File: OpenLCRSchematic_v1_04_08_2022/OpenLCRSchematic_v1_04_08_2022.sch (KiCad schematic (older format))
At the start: 18 parts

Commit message: Measurement Circuit Update
Update measurement circuit
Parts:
- removed U?: TLC7528CN, DIP254P762X508-20, symbol TLC7528CN:TLC7528CN
- removed U?: MCP6294-E_SL, SOIC127P600X175-14N, symbol MCP6294-E_SL:MCP6294-E_SL
- removed U?: CD74HCT4066M, SOIC127P600X175-14N, symbol CD74HCT4066M:CD74HCT4066M
- removed U?: MCP6S91-E_P, DIP787W46P254L927H533Q8, symbol MCP6S91-E_P:MCP6S91-E_P
- removed U?: INA217AIP, DIP794W45P254L959H508Q8, symbol INA217AIP:INA217AIP
- gave numbers to parts that had none: 13
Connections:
- net labels added: +3.3V, +BATT, 3.3V
- wire segments 66 -> 67
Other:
- note added: "Measurement Circuit"
- note added: "Note: 3.3V is generated by a\nlinear regulator on the Teensy \n4.1 board derived from 5V."
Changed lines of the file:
@@
 $Descr A4 11693 8268
 encoding utf-8
-Sheet 1 1
+Sheet 1 2
 Title "OpenLCR Measurement Circuitry"
 Date ""
@@
 $EndDescr
 $Comp
-L TLC7528CN:TLC7528CN U?
-U 1 1 6250931A
-P 17700 4750
-F 0 "U?" H 17700 6020 50  0000 C CNN
-F 1 "TLC7528CN" H 17700 5929 50  0000 C CNN
-F 2 "DIP254P762X508-20" H 17700 4750 50  0001 L BNN
-F 3 "" H 17700 4750 50  0001 L BNN
-F 4 "PDIP-20" H 17700 4750 50  0001 L BNN "PACKAGE"
-F 5 "36K3648" H 17700 4750 50  0001 L BNN "OC_NEWARK"
-F 6 "TLC7528CN" H 17700 4750 50  0001 L BNN "MPN"
-F 7 "8454647" H 17700 4750 50  0001 L BNN "OC_FARNELL"
-F 8 "Texas Instruments" H 17700 4750 50  0001 L BNN "SUPPLIER"
-	1    17700 4750
-	1    0    0    -1
-$EndComp
-$Comp
-L MCP6294-E_SL:MCP6294-E_SL U?
-U 1 1 6250B959
-P 19950 4500
-F 0 "U?" H 19950 5370 50  0000 C CNN
-F 1 "MCP6294-E_SL" H 19950 5279 50  0000 C CNN
-F 2 "SOIC127P600X175-14N" H 19950 4500 50  0001 L BNN
-F 3 "" H 19950 4500 50  0001 L BNN
-	1    19950 4500
-	1    0    0    -1
-$EndComp
-$Comp
-L CD74HCT4066M:CD74HCT4066M U?
-U 1 1 6250CB78
-P 19950 6250
-F 0 "U?" H 19950 7120 50  0000 C CNN
-F 1 "CD74HCT4066M" H 19950 7029 50  0000 C CNN
-F 2 "SOIC127P600X175-14N" H 19950 6250 50  0001 L BNN
-F 3 "" H 19950 6250 50  0001 L BNN
-	1    19950 6250
-	1    0    0    -1
-$EndComp
-$Comp
-L MCP6S91-E_P:MCP6S91-E_P U?
-U 1 1 6250E62B
-P 19950 2400
-F 0 "U?" H 19950 3170 50  0000 C CNN
-F 1 "MCP6S91-E_P" H 19950 3079 50  0000 C CNN
-F 2 "DIP787W46P254L927H533Q8" H 19950 2400 50  0001 L BNN
-F 3 "" H 19950 2400 50  0001 L BNN
-	1    19950 2400
-	1    0    0    -1
-$EndComp
-$Comp
-L INA217AIP:INA217AIP U?
-U 1 1 6250F06B
-P 23600 3850
-F 0 "U?" H 23600 4620 50  0000 C CNN
-F 1 "INA217AIP" H 23600 4529 50  0000 C CNN
-F 2 "DIP794W45P254L959H508Q8" H 23600 3850 50  0001 L BNN
-F 3 "" H 23600 3850 50  0001 L BNN
-	1    23600 3850
-	1    0    0    -1
-$EndComp
-$Comp
-L MAX680CPA_:MAX680CPA+ U?
+L MAX680CPA_:MAX680CPA+ U2
 U 1 1 6250FB8A
 P 2000 3850
-F 0 "U?" H 2000 4620 50  0000 C CNN
+F 0 "U2" H 2000 4620 50  0000 C CNN
 F 1 "MAX680CPA+" H 2000 4529 50  0000 C CNN
 F 2 "DIP794W47P254L991H457Q8" H 2000 3850 50  0001 L BNN
@@
 $EndComp
 $Comp
-L LiPoCharger_Booster:LiPoChargeBoost U?
+L LiPoCharger_Booster:LiPoChargeBoost U1
 U 1 1 62518618
 P 3000 2400
-F 0 "U?" H 3000 2725 50  0000 C CNN
+F 0 "U1" H 3000 2725 50  0000 C CNN
 F 1 "LiPoChargeBoost" H 3000 2634 50  0000 C CNN
 F 2 "" H 3000 2700 50  0001 C CNN
@@
 Lithium-Polymer Battery\n3.7V-4.2V, 2500mAh\nContains internal\nprotection circuitry
 $Comp
-L Device:Battery_Cell BT?
+L Device:Battery_Cell BT1
 U 1 1 62515AE1
 P 1650 2500
-F 0 "BT?" H 1768 2596 50  0000 L CNN
+F 0 "BT1" H 1768 2596 50  0000 L CNN
 F 1 "Battery_Cell" H 1768 2505 50  0000 L CNN
 F 2 "" V 1650 2560 50  0001 C CNN
@@
 	3600 2300 4150 2300
 $Comp
-L MAX680CPA_:MAX680CPA+ U?
+L MAX680CPA_:MAX680CPA+ U3
 U 1 1 6251CE4F
 P 2000 5300
-F 0 "U?" H 2000 6070 50  0000 C CNN
+F 0 "U3" H 2000 6070 50  0000 C CNN
 F 1 "MAX680CPA+" H 2000 5979 50  0000 C CNN
 F 2 "DIP794W47P254L991H457Q8" H 2000 5300 50  0001 L BNN
@@
 $EndComp
 $Comp
-L MAX680CPA_:MAX680CPA+ U?
+L MAX680CPA_:MAX680CPA+ U4
 U 1 1 6251D7F3
 P 2000 6800
-F 0 "U?" H 2000 7570 50  0000 C CNN
+F 0 "U4" H 2000 7570 50  0000 C CNN
 F 1 "MAX680CPA+" H 2000 7479 50  0000 C CNN
 F 2 "DIP794W47P254L991H457Q8" H 2000 6800 50  0001 L BNN
@@
 GND
 $Comp
-L power:+5V #PWR?
+L power:+5V #PWR03
 U 1 1 6251E328
 P 4300 2400
-F 0 "#PWR?" H 4300 2250 50  0001 C CNN
+F 0 "#PWR03" H 4300 2250 50  0001 C CNN
 F 1 "+5V" H 4315 2573 50  0000 C CNN
 F 2 "" H 4300 2400 50  0001 C CNN
@@
 $EndComp
 $Comp
-L power:GND #PWR?
+L power:GND #PWR04
 U 1 1 6251ED8F
 P 4300 2500
-F 0 "#PWR?" H 4300 2250 50  0001 C CNN
+F 0 "#PWR04" H 4300 2250 50  0001 C CNN
 F 1 "GND" H 4305 2327 50  0000 C CNN
 F 2 "" H 4300 2500 50  0001 C CNN
@@
 	3600 2500 4300 2500
 $Comp
-L power:GND #PWR?
+L power:GND #PWR09
 U 1 1 6251F89D
 P 2850 4250
-F 0 "#PWR?" H 2850 4000 50  0001 C CNN
+F 0 "#PWR09" H 2850 4000 50  0001 C CNN
 F 1 "GND" H 2855 4077 50  0000 C CNN
 F 2 "" H 2850 4250 50  0001 C CNN
@@
 $EndComp
 $Comp
-L power:GND #PWR?
+L power:GND #PWR011
 U 1 1 625204F9
 P 2850 5700
-F 0 "#PWR?" H 2850 5450 50  0001 C CNN
+F 0 "#PWR011" H 2850 5450 50  0001 C CNN
 F 1 "GND" H 2855 5527 50  0000 C CNN
 F 2 "" H 2850 5700 50  0001 C CNN
@@
 $EndComp
 $Comp
-L power:GND #PWR?
+L power:GND #PWR013
 U 1 1 625209A4
 P 2850 7200
-F 0 "#PWR?" H 2850 6950 50  0001 C CNN
+F 0 "#PWR013" H 2850 6950 50  0001 C CNN
 F 1 "GND" H 2855 7027 50  0000 C CNN
 F 2 "" H 2850 7200 50  0001 C CNN
@@
 $EndComp
 $Comp
-L power:+5V #PWR?
+L power:+5V #PWR012
 U 1 1 62520C44
 P 2850 6400
-F 0 "#PWR?" H 2850 6250 50  0001 C CNN
+F 0 "#PWR012" H 2850 6250 50  0001 C CNN
 F 1 "+5V" H 2865 6573 50  0000 C CNN
 F 2 "" H 2850 6400 50  0001 C CNN
@@
 $EndComp
 $Comp
-L power:+5V #PWR?
+L power:+5V #PWR010
 U 1 1 62521D7D
 P 2850 4900
-F 0 "#PWR?" H 2850 4750 50  0001 C CNN
+F 0 "#PWR010" H 2850 4750 50  0001 C CNN
 F 1 "+5V" H 2865 5073 50  0000 C CNN
 F 2 "" H 2850 4900 50  0001 C CNN
@@
 $EndComp
 $Comp
-L power:+5V #PWR?
+L power:+5V #PWR06
 U 1 1 62521EFB
 P 2850 3450
-F 0 "#PWR?" H 2850 3300 50  0001 C CNN
+F 0 "#PWR06" H 2850 3300 50  0001 C CNN
 F 1 "+5V" H 2865 3623 50  0000 C CNN
 F 2 "" H 2850 3450 50  0001 C CNN
@@
 -10V
 $Comp
-L power:GND #PWR?
+L power:GND #PWR07
 U 1 1 62527CB2
 P 3200 3650
-F 0 "#PWR?" H 3200 3400 50  0001 C CNN
+F 0 "#PWR07" H 3200 3400 50  0001 C CNN
 F 1 "GND" H 3205 3477 50  0000 C CNN
 F 2 "" H 3200 3650 50  0001 C CNN
@@
 	3200 3650 3500 3650
 $Comp
-L Device:CP C?
+L Device:CP C1
 U 1 1 6252898D
 P 3500 3400
-F 0 "C?" H 3618 3446 50  0000 L CNN
+F 0 "C1" H 3618 3446 50  0000 L CNN
 F 1 "10u" H 3618 3355 50  0000 L CNN
 F 2 "" H 3538 3250 50  0001 C CNN
@@
 $EndComp
 $Comp
-L Device:CP C?
+L Device:CP C3
 U 1 1 6252958A
 P 3500 3900
-F 0 "C?" H 3618 3946 50  0000 L CNN
+F 0 "C3" H 3618 3946 50  0000 L CNN
 F 1 "10u" H 3618 3855 50  0000 L CNN
 F 2 "" H 3538 3750 50  0001 C CNN
@@
 	3500 3250 3500 3150
 $Comp
-L Device:CP C?
+L Device:CP C2
 U 1 1 6252C5D6
 P 1150 3700
-F 0 "C?" H 950 3750 50  0000 L CNN
+F 0 "C2" H 950 3750 50  0000 L CNN
 F 1 "10u" H 900 3650 50  0000 L CNN
 F 2 "" H 1188 3550 50  0001 C CNN
@@
 $EndComp
 $Comp
-L Device:CP C?
+L Device:CP C4
 U 1 1 625314A6
 P 950 4000
-F 0 "C?" H 750 4050 50  0000 L CNN
+F 0 "C4" H 750 4050 50  0000 L CNN
 F 1 "10u" H 700 3950 50  0000 L CNN
 F 2 "" H 988 3850 50  0001 C CNN
@@
 	1100 4050 1300 4050
 $Comp
-L Device:CP C?
+L Device:CP C5
 U 1 1 62535813
 P 1150 5150
-F 0 "C?" H 950 5200 50  0000 L CNN
+F 0 "C5" H 950 5200 50  0000 L CNN
 F 1 "10u" H 900 5100 50  0000 L CNN
 F 2 "" H 1188 5000 50  0001 C CNN
@@
 $EndComp
 $Comp
-L Device:CP C?
+L Device:CP C6
 U 1 1 62535819
 P 950 5450
-F 0 "C?" H 750 5500 50  0000 L CNN
+F 0 "C6" H 750 5500 50  0000 L CNN
 F 1 "10u" H 700 5400 50  0000 L CNN
 F 2 "" H 988 5300 50  0001 C CNN
@@
 	1100 5500 1300 5500
 $Comp
-L Device:CP C?
+L Device:CP C7
 U 1 1 62537749
 P 1150 6650
-F 0 "C?" H 950 6700 50  0000 L CNN
+F 0 "C7" H 950 6700 50  0000 L CNN
 F 1 "10u" H 900 6600 50  0000 L CNN
 F 2 "" H 1188 6500 50  0001 C CNN
@@
 $EndComp
 $Comp
-L Device:CP C?
+L Device:CP C8
 U 1 1 6253774F
 P 950 6950
-F 0 "C?" H 750 7000 50  0000 L CNN
+F 0 "C8" H 750 7000 50  0000 L CNN
 F 1 "10u" H 700 6900 50  0000 L CNN
 F 2 "" H 988 6800 50  0001 C CNN
@@
 	4550 7750 4550 500
 Wire Notes Line width 39
-	4550 500  500  500
+	500  7750 4550 7750
+Wire Wire Line
+	3500 1600 4000 1600
+Text Label 3650 1600 0    50   ~ 0
+3.3V
+Text Notes 3200 1900 0    50   ~ 0
+Note:  3.3V is generated by a\nlinear regulator on the Teensy \n4.1 board derived from 5V.
+$Comp
+L power:+3.3V #PWR01
+U 1 1 6259A3DF
+P 4000 1600
+F 0 "#PWR01" H 4000 1450 50  0001 C CNN
+F 1 "+3.3V" H 4015 1773 50  0000 C CNN
+F 2 "" H 4000 1600 50  0001 C CNN
+F 3 "" H 4000 1600 50  0001 C CNN
+	1    4000 1600
+	1    0    0    -1
+$EndComp
+$Sheet
+S 4700 1050 6350 1700
+U 625D4E84
+F0 "Measurement Circuit" 50
+F1 "MeasurementCircuit.sch" 50
+$EndSheet
+Text Notes 4700 850  0    157  ~ 31
+Measurement Circuit
 Wire Notes Line width 39
-	500  7750 4550 7750
+	11150 2900 4550 2900
+Wire Notes Line width 39
+	11150 500  11150 2900
+Wire Notes Line width 39
+	500  500  11150 500
+$Comp
+L power:+10V #PWR05
+U 1 1 625FFB3F
+P 3500 3150
+F 0 "#PWR05" H 3500 3000 50  0001 C CNN
+F 1 "+10V" H 3515 3323 50  0000 C CNN
+F 2 "" H 3500 3150 50  0001 C CNN
+F 3 "" H 3500 3150 50  0001 C CNN
+	1    3500 3150
+	1    0    0    -1
+$EndComp
+Connection ~ 3500 3150
+$Comp
+L power:-10V #PWR08
+U 1 1 6260017C
+P 3500 4150
+F 0 "#PWR08" H 3500 4250 50  0001 C CNN
+F 1 "-10V" H 3515 4323 50  0000 C CNN
+F 2 "" H 3500 4150 50  0001 C CNN
+F 3 "" H 3500 4150 50  0001 C CNN
+	1    3500 4150
+	-1   0    0    1
+$EndComp
+Connection ~ 3500 4150
+$Comp
+L power:+BATT #PWR02
+U 1 1 626C0E5D
+P 4150 2300
+F 0 "#PWR02" H 4150 2150 50  0001 C CNN
+F 1 "+BATT" H 4165 2473 50  0000 C CNN
+F 2 "" H 4150 2300 50  0001 C CNN
+F 3 "" H 4150 2300 50  0001 C CNN
+	1    4150 2300
+	1    0    0    -1
+$EndComp
 $EndSCHEMATC

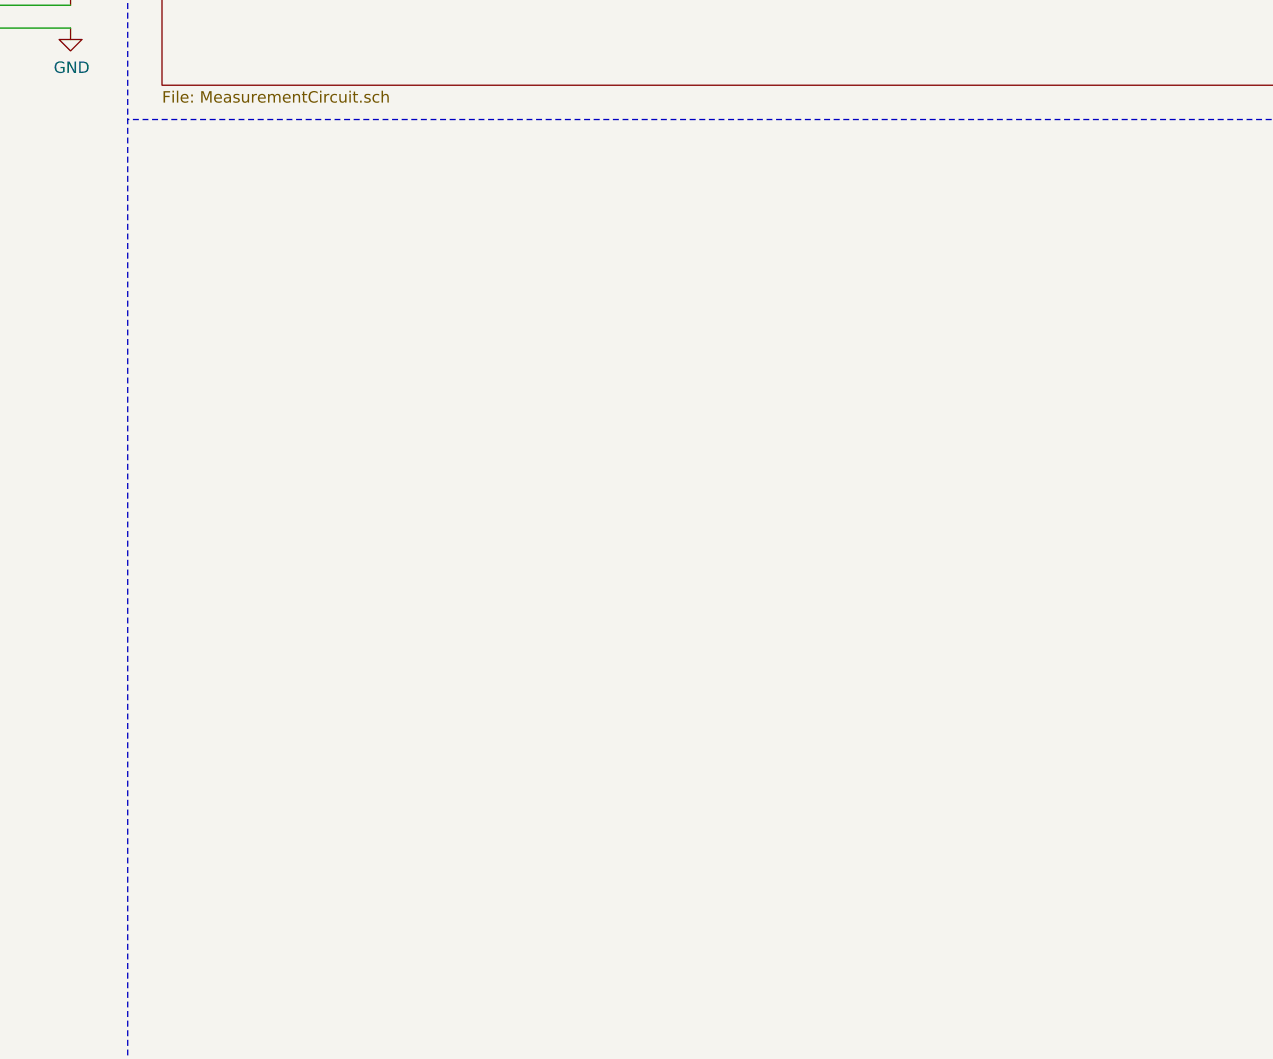
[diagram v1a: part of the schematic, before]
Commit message: Make Teensy 4.1 symbol
Add the Teensy 4.1 circuit symbol to the schematic.  Still not exactly sure on what pin assignments I'll use.
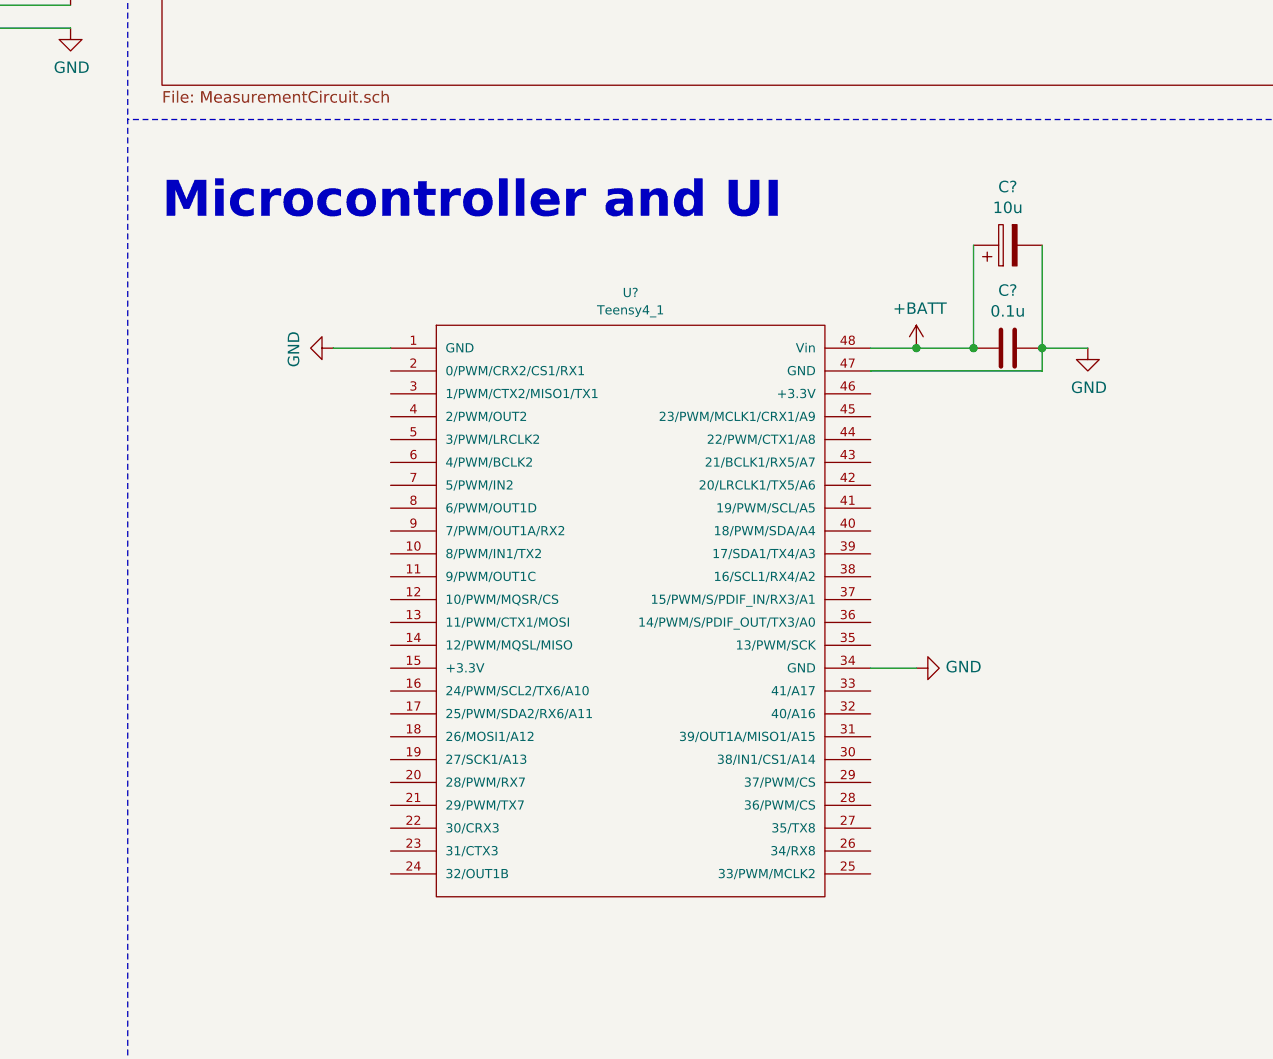
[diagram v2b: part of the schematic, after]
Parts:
- added C?: 10u, symbol Device:CP
- added C?: 0.1u, symbol Device:C
- added U?: Teensy4_1, symbol Teensy4_1:Teensy4_1
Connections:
- wire segments 67 -> 76
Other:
- note added: "Microcontroller and UI"
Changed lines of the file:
@@
 	1    0    0    -1
 $EndComp
+$Comp
+L Teensy4_1:Teensy4_1 U?
+U 1 1 6299E2B7
+P 6750 5150
+F 0 "U?" H 6750 6642 40  0000 C CNN
+F 1 "Teensy4_1" H 6750 6566 40  0000 C CNN
+F 2 "" H 6750 6550 40  0001 C CNN
+F 3 "" H 6750 6550 40  0001 C CNN
+	1    6750 5150
+	1    0    0    -1
+$EndComp
+Text Notes 4700 3350 0    157  ~ 31
+Microcontroller and UI
+$Comp
+L power:+BATT #PWR?
+U 1 1 629A203F
+P 8000 3900
+F 0 "#PWR?" H 8000 3750 50  0001 C CNN
+F 1 "+BATT" H 8015 4073 50  0000 C CNN
+F 2 "" H 8000 3900 50  0001 C CNN
+F 3 "" H 8000 3900 50  0001 C CNN
+	1    8000 3900
+	1    0    0    -1
+$EndComp
+$Comp
+L Device:CP C?
+U 1 1 629A283D
+P 8400 3450
+F 0 "C?" V 8655 3450 50  0000 C CNN
+F 1 "10u" V 8564 3450 50  0000 C CNN
+F 2 "" H 8438 3300 50  0001 C CNN
+F 3 "~" H 8400 3450 50  0001 C CNN
+	1    8400 3450
+	0    -1   -1   0
+$EndComp
+$Comp
+L Device:C C?
+U 1 1 629A3784
+P 8400 3900
+F 0 "C?" V 8148 3900 50  0000 C CNN
+F 1 "0.1u" V 8239 3900 50  0000 C CNN
+F 2 "" H 8438 3750 50  0001 C CNN
+F 3 "~" H 8400 3900 50  0001 C CNN
+	1    8400 3900
+	0    1    1    0
+$EndComp
+$Comp
+L power:GND #PWR?
+U 1 1 629A5333
+P 8750 3900
+F 0 "#PWR?" H 8750 3650 50  0001 C CNN
+F 1 "GND" H 8755 3727 50  0000 C CNN
+F 2 "" H 8750 3900 50  0001 C CNN
+F 3 "" H 8750 3900 50  0001 C CNN
+	1    8750 3900
+	1    0    0    -1
+$EndComp
+Wire Wire Line
+	8250 3900 8000 3900
+Wire Wire Line
+	8000 3900 7800 3900
+Connection ~ 8000 3900
+Wire Wire Line
+	8250 3900 8250 3450
+Connection ~ 8250 3900
+Wire Wire Line
+	8550 3450 8550 3900
+Wire Wire Line
+	8550 3900 8750 3900
+Connection ~ 8550 3900
+$Comp
+L power:GND #PWR?
+U 1 1 629ADD22
+P 5450 3900
+F 0 "#PWR?" H 5450 3650 50  0001 C CNN
+F 1 "GND" H 5455 3727 50  0000 C CNN
+F 2 "" H 5450 3900 50  0001 C CNN
+F 3 "" H 5450 3900 50  0001 C CNN
+	1    5450 3900
+	0    1    1    0
+$EndComp
+Wire Wire Line
+	7800 4000 8550 4000
+Wire Wire Line
+	8550 4000 8550 3900
+$Comp
+L power:GND #PWR?
+U 1 1 629B1BE9
+P 8000 5300
+F 0 "#PWR?" H 8000 5050 50  0001 C CNN
+F 1 "GND" V 8005 5172 50  0000 R CNN
+F 2 "" H 8000 5300 50  0001 C CNN
+F 3 "" H 8000 5300 50  0001 C CNN
+	1    8000 5300
+	0    -1   -1   0
+$EndComp
+Wire Wire Line
+	8000 5300 7800 5300
+Wire Wire Line
+	5450 3900 5700 3900
 $EndSCHEMATC

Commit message: Add Connections to Microcontroller
Add ILI9341 display and microcontroller connections.
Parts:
- added R?: 100, symbol Device:R_US
- added U?: ILI9341_Display, symbol ILI9341_Display_Module:ILI9341_Display
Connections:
- net labels added: CURRENT_MONITOR_SIGNAL_TO_ADC, D0, D1, D2, D3, D4, D5, D6, D7, DACSelAbar, DAC_CSbar, DAC_OUTPUT_MONITOR_SIGNAL_TO_ADC, DAC_WRbar, DISPLAY_CS, DISPLAY_DC, DISPLAY_MISO, DISPLAY_MOSI, DISPLAY_SCK, PGA_MOSI, PGA_SCK, PGA_~CS, SW1EN, SW2EN, SW3EN, SW4EN, SW5EN, SW6EN, SW7EN, SW8EN, TOUCHSCREEN_CS, TOUCHSCREEN_IRQ, VOLTAGE_MONITOR_SIGNAL_TO_ADC
- wire segments 76 -> 134

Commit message: Update Readme
Update readme with a short description of the design
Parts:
- gave numbers to parts that had none: 5
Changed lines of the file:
@@
 $EndComp
 $Comp
-L Teensy4_1:Teensy4_1 U?
+L Teensy4_1:Teensy4_1 U12
 U 1 1 6299E2B7
 P 6750 5150
-F 0 "U?" H 6750 6642 40  0000 C CNN
+F 0 "U12" H 6750 6642 40  0000 C CNN
 F 1 "Teensy4_1" H 6750 6566 40  0000 C CNN
 F 2 "" H 6750 6550 40  0001 C CNN
@@
 Microcontroller and UI
 $Comp
-L power:+BATT #PWR?
+L power:+BATT #PWR054
 U 1 1 629A203F
 P 8000 3900
-F 0 "#PWR?" H 8000 3750 50  0001 C CNN
+F 0 "#PWR054" H 8000 3750 50  0001 C CNN
 F 1 "+BATT" H 8015 4073 50  0000 C CNN
 F 2 "" H 8000 3900 50  0001 C CNN
@@
 $EndComp
 $Comp
-L Device:CP C?
+L Device:CP C21
 U 1 1 629A283D
 P 8400 3450
-F 0 "C?" V 8655 3450 50  0000 C CNN
+F 0 "C21" V 8655 3450 50  0000 C CNN
 F 1 "10u" V 8564 3450 50  0000 C CNN
 F 2 "" H 8438 3300 50  0001 C CNN
@@
 $EndComp
 $Comp
-L Device:C C?
+L Device:C C22
 U 1 1 629A3784
 P 8400 3900
-F 0 "C?" V 8148 3900 50  0000 C CNN
+F 0 "C22" V 8148 3900 50  0000 C CNN
 F 1 "0.1u" V 8239 3900 50  0000 C CNN
 F 2 "" H 8438 3750 50  0001 C CNN
@@
 $EndComp
 $Comp
-L power:GND #PWR?
+L power:GND #PWR055
 U 1 1 629A5333
 P 8750 3900
-F 0 "#PWR?" H 8750 3650 50  0001 C CNN
+F 0 "#PWR055" H 8750 3650 50  0001 C CNN
 F 1 "GND" H 8755 3727 50  0000 C CNN
 F 2 "" H 8750 3900 50  0001 C CNN
@@
 Connection ~ 8550 3900
 $Comp
-L power:GND #PWR?
+L power:GND #PWR053
 U 1 1 629ADD22
 P 5600 3900
-F 0 "#PWR?" H 5600 3650 50  0001 C CNN
+F 0 "#PWR053" H 5600 3650 50  0001 C CNN
 F 1 "GND" H 5605 3727 50  0000 C CNN
 F 2 "" H 5600 3900 50  0001 C CNN
@@
 	8550 4000 8550 3900
 $Comp
-L power:GND #PWR?
+L power:GND #PWR061
 U 1 1 629B1BE9
 P 8000 5300
-F 0 "#PWR?" H 8000 5050 50  0001 C CNN
+F 0 "#PWR061" H 8000 5050 50  0001 C CNN
 F 1 "GND" V 8005 5172 50  0000 R CNN
 F 2 "" H 8000 5300 50  0001 C CNN
@@
 	8000 5300 7800 5300
 $Comp
-L ILI9341_Display_Module:ILI9341_Display U?
+L ILI9341_Display_Module:ILI9341_Display U13
 U 1 1 629BBAF9
 P 10750 5550
-F 0 "U?" H 10700 6500 40  0000 L CNN
+F 0 "U13" H 10700 6500 40  0000 L CNN
 F 1 "ILI9341_Display" H 10500 6400 40  0000 L CNN
 F 2 "" H 10750 6350 40  0001 C CNN
@@
 $EndComp
 $Comp
-L power:+BATT #PWR?
+L power:+BATT #PWR057
 U 1 1 629BD32A
 P 10100 4900
-F 0 "#PWR?" H 10100 4750 50  0001 C CNN
+F 0 "#PWR057" H 10100 4750 50  0001 C CNN
 F 1 "+BATT" H 10115 5073 50  0000 C CNN
 F 2 "" H 10100 4900 50  0001 C CNN
@@
 $EndComp
 $Comp
-L power:GND #PWR?
+L power:GND #PWR058
 U 1 1 629BD7C1
 P 10100 5000
-F 0 "#PWR?" H 10100 4750 50  0001 C CNN
+F 0 "#PWR058" H 10100 4750 50  0001 C CNN
 F 1 "GND" V 10105 4872 50  0000 R CNN
 F 2 "" H 10100 5000 50  0001 C CNN
@@
 	10200 5100 9500 5100
 $Comp
-L power:+3.3V #PWR?
+L power:+3.3V #PWR056
 U 1 1 629D4F96
 P 8000 4100
-F 0 "#PWR?" H 8000 3950 50  0001 C CNN
+F 0 "#PWR056" H 8000 3950 50  0001 C CNN
 F 1 "+3.3V" V 7950 4250 50  0000 L CNN
 F 2 "" H 8000 4100 50  0001 C CNN
@@
 	8000 4100 7800 4100
 $Comp
-L power:+3.3V #PWR?
+L power:+3.3V #PWR060
 U 1 1 629D8062
 P 5450 5300
-F 0 "#PWR?" H 5450 5150 50  0001 C CNN
+F 0 "#PWR060" H 5450 5150 50  0001 C CNN
 F 1 "+3.3V" V 5465 5428 50  0000 L CNN
 F 2 "" H 5450 5300 50  0001 C CNN
@@
 	5450 5300 5700 5300
 $Comp
-L power:+3.3V #PWR?
+L power:+3.3V #PWR059
 U 1 1 629DAB80
 P 10100 5200
-F 0 "#PWR?" H 10100 5050 50  0001 C CNN
+F 0 "#PWR059" H 10100 5050 50  0001 C CNN
 F 1 "+3.3V" V 10115 5328 50  0000 L CNN
 F 2 "" H 10100 5200 50  0001 C CNN
@@
 	10200 5500 9650 5500
 $Comp
-L power:+BATT #PWR?
+L power:+BATT #PWR062
 U 1 1 629E4CE1
 P 9500 5600
-F 0 "#PWR?" H 9500 5450 50  0001 C CNN
+F 0 "#PWR062" H 9500 5450 50  0001 C CNN
 F 1 "+BATT" V 9515 5727 50  0000 L CNN
 F 2 "" H 9500 5600 50  0001 C CNN
@@
 $EndComp
 $Comp
-L Device:R_US R?
+L Device:R_US R22
 U 1 1 629E5ADE
 P 9850 5600
-F 0 "R?" V 9900 5700 50  0000 L CNN
+F 0 "R22" V 9900 5700 50  0000 L CNN
 F 1 "100" V 9900 5300 50  0000 L CNN
 F 2 "" V 9890 5590 50  0001 C CNN
